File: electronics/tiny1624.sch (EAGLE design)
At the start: 9 parts, among them U1 ATTINY1624

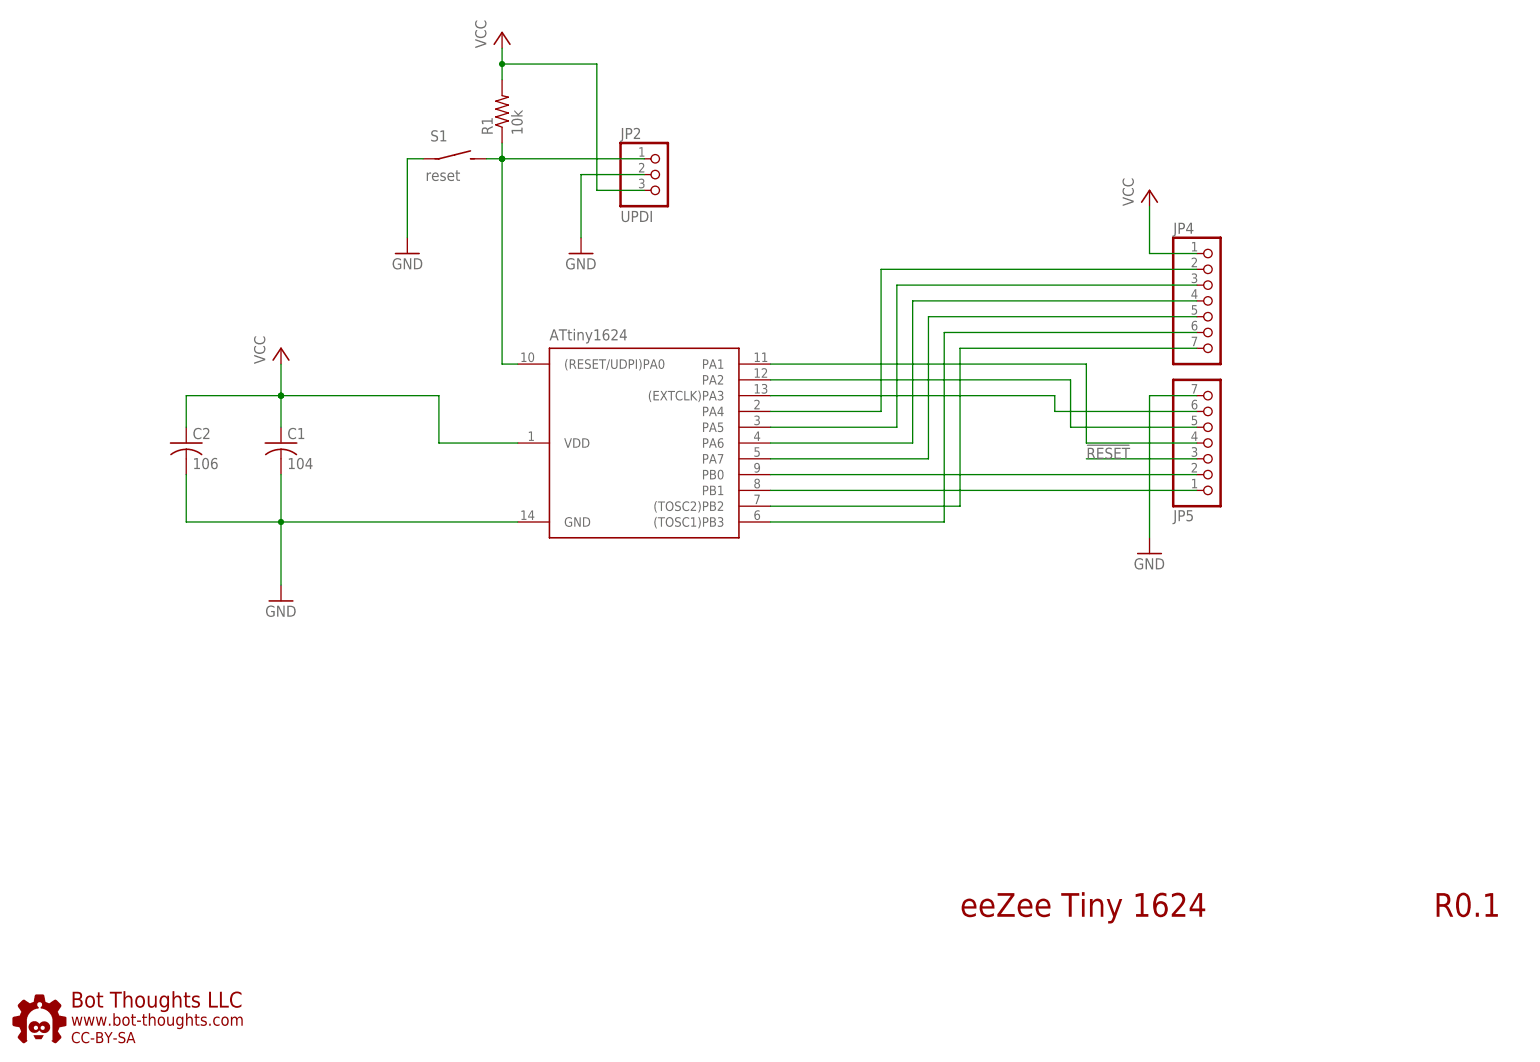
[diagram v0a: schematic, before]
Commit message: Updated reset circuit, added example blink code
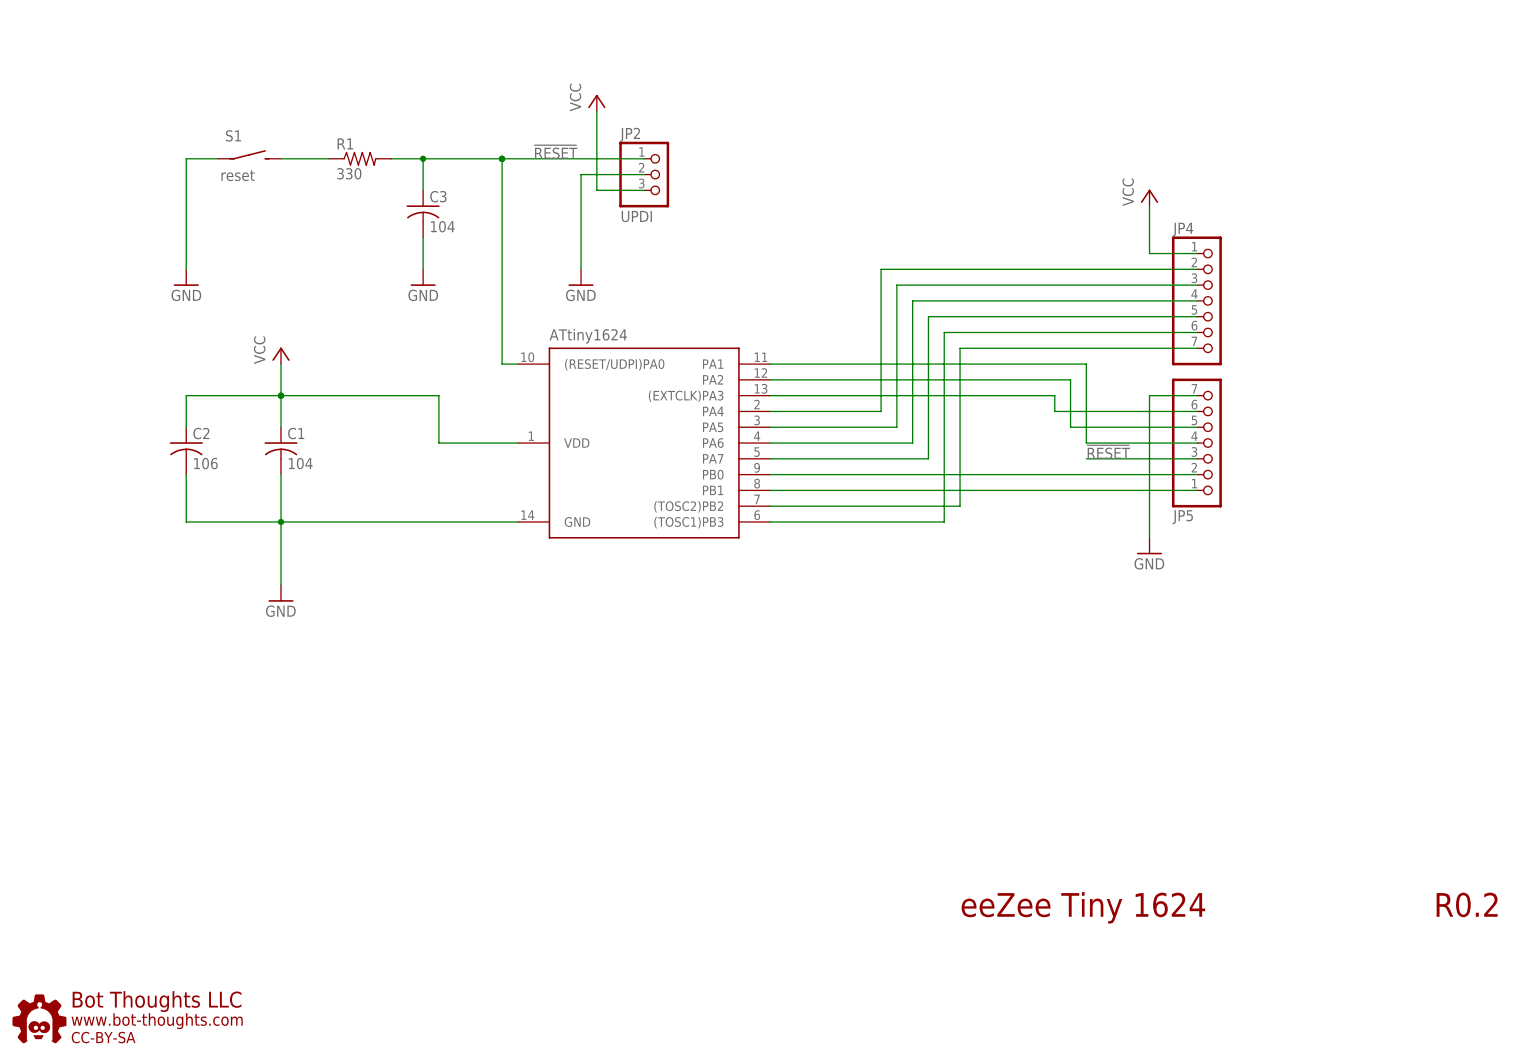
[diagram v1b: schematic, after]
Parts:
- added C3: 104, bt_rcl:C-0603
- R1: value 10k -> 330
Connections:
- new net N$12: R1.1, S1.S
- net !RESET: now also C3.+, R1.2; no longer R1.1, S1.S
- net GND: now also C3.-
- net VCC: no longer R1.2
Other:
- note added: "R0.2"
- note removed: "R0.1"
- moved on the sheet: R1, S1
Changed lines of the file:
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@@
 <part name="GND3" library="supply1" deviceset="GND" device=""/>
 <part name="P+2" library="supply1" deviceset="VCC" device=""/>
-<part name="R1" library="rcl" deviceset="R-US_" device="R0603" value="10k">
+<part name="R1" library="rcl" deviceset="R-US_" device="R0603" value="330">
 <attribute name="PARTNO" value="ERJ-3GEYJ103V"/>
 </part>
@@
 <part name="U1" library="bt_avr" deviceset="ATTINY1624" device="-SSU" value="ATTINY1624"/>
 <part name="JP2" library="pinhead-2" deviceset="PINHD-1X03" device="_2.54-S" value="UPDI"/>
+<part name="C3" library="bt_rcl" deviceset="C" device="-0603" value="104">
+<attribute name="BOM" value="EXCLUDE"/>
+<attribute name="PARTNO" value="0603YC104KAT2A"/>
+</part>
+<part name="GND1" library="supply1" deviceset="GND" device=""/>
 </parts>
 <sheets>
@@
 <plain>
 <text x="154.94" y="22.86" size="3.81" layer="94">eeZee Tiny 1624</text>
-<text x="231.14" y="22.86" size="3.81" layer="94">R0.1</text>
+<text x="231.14" y="22.86" size="3.81" layer="94">R0.2</text>
 </plain>
 <instances>
-<instance part="P+1" gate="VCC" x="81.28" y="165.1"/>
-<instance part="GND2" gate="1" x="93.98" y="129.54"/>
+<instance part="P+1" gate="VCC" x="96.52" y="154.94"/>
+<instance part="GND2" gate="1" x="93.98" y="124.46"/>
 <instance part="C1" gate="G$1" x="45.72" y="99.06">
 <attribute name="PARTNO" value="0603YC104KAT2A" x="45.72" y="99.06" size="1.778" layer="96" display="off"/>
 <attribute name="BOM" value="EXCLUDE" x="45.72" y="99.06" size="1.778" layer="96" display="off"/>
 </instance>
-<instance part="GND3" gate="1" x="66.04" y="129.54" rot="MR0"/>
+<instance part="GND3" gate="1" x="30.48" y="124.46" rot="MR0"/>
 <instance part="P+2" gate="VCC" x="45.72" y="114.3"/>
-<instance part="R1" gate="G$1" x="81.28" y="152.4" rot="R90">
-<attribute name="PARTNO" value="ERJ-3GEYJ103V" x="81.28" y="152.4" size="1.778" layer="96" display="off"/>
+<instance part="R1" gate="G$1" x="58.42" y="144.78">
+<attribute name="PARTNO" value="ERJ-3GEYJ103V" x="58.42" y="144.78" size="1.778" layer="96" rot="R270" display="off"/>
 </instance>
 <instance part="P+4" gate="VCC" x="185.42" y="139.7"/>
@@
 <instance part="JP5" gate="A" x="195.58" y="99.06" rot="MR180"/>
 <instance part="GND4" gate="1" x="185.42" y="81.28"/>
-<instance part="S1" gate="S1" x="73.66" y="144.78"/>
+<instance part="S1" gate="S1" x="40.64" y="144.78"/>
 <instance part="U$1" gate="G$1" x="2.54" y="2.54"/>
 <instance part="U1" gate="G$1" x="104.14" y="99.06"/>
 <instance part="JP2" gate="A" x="106.68" y="142.24"/>
+<instance part="C3" gate="C1" x="68.58" y="137.16">
+<attribute name="PARTNO" value="0603YC104KAT2A" x="68.58" y="137.16" size="1.778" layer="96" display="off"/>
+<attribute name="BOM" value="EXCLUDE" x="68.58" y="137.16" size="1.778" layer="96" display="off"/>
+</instance>
+<instance part="GND1" gate="1" x="68.58" y="124.46" rot="MR0"/>
 </instances>
 <busses>
@@
 <net name="GND" class="0">
 <segment>
-<wire x1="93.98" y1="142.24" x2="93.98" y2="132.08" width="0.1524" layer="91"/>
+<wire x1="93.98" y1="142.24" x2="93.98" y2="127" width="0.1524" layer="91"/>
 <pinref part="GND2" gate="1" pin="GND"/>
 <pinref part="JP2" gate="A" pin="2"/>
@@
 <segment>
 <pinref part="GND3" gate="1" pin="GND"/>
-<wire x1="68.58" y1="144.78" x2="66.04" y2="144.78" width="0.1524" layer="91"/>
-<wire x1="66.04" y1="144.78" x2="66.04" y2="132.08" width="0.1524" layer="91"/>
+<wire x1="35.56" y1="144.78" x2="30.48" y2="144.78" width="0.1524" layer="91"/>
+<wire x1="30.48" y1="144.78" x2="30.48" y2="127" width="0.1524" layer="91"/>
 <pinref part="S1" gate="S1" pin="P"/>
 </segment>
@@
 <wire x1="185.42" y1="106.68" x2="185.42" y2="83.82" width="0.1524" layer="91"/>
 <pinref part="GND4" gate="1" pin="GND"/>
+</segment>
+<segment>
+<pinref part="C3" gate="C1" pin="-"/>
+<pinref part="GND1" gate="1" pin="GND"/>
+<wire x1="68.58" y1="127" x2="68.58" y2="132.08" width="0.1524" layer="91"/>
 </segment>
 </net>
@@
 </segment>
 <segment>
-<wire x1="81.28" y1="157.48" x2="81.28" y2="160.02" width="0.1524" layer="91"/>
 <pinref part="P+1" gate="VCC" pin="VCC"/>
-<pinref part="R1" gate="G$1" pin="2"/>
 <pinref part="JP2" gate="A" pin="3"/>
-<wire x1="81.28" y1="160.02" x2="81.28" y2="162.56" width="0.1524" layer="91"/>
 <wire x1="104.14" y1="139.7" x2="96.52" y2="139.7" width="0.1524" layer="91"/>
-<wire x1="96.52" y1="139.7" x2="96.52" y2="160.02" width="0.1524" layer="91"/>
-<wire x1="81.28" y1="160.02" x2="96.52" y2="160.02" width="0.1524" layer="91"/>
-<junction x="81.28" y="160.02"/>
+<wire x1="96.52" y1="139.7" x2="96.52" y2="152.4" width="0.1524" layer="91"/>
 </segment>
 <segment>
@@
 <net name="!RESET" class="0">
 <segment>
-<wire x1="81.28" y1="144.78" x2="81.28" y2="147.32" width="0.1524" layer="91"/>
 <junction x="81.28" y="144.78"/>
-<pinref part="R1" gate="G$1" pin="1"/>
 <wire x1="104.14" y1="144.78" x2="81.28" y2="144.78" width="0.1524" layer="91"/>
-<wire x1="78.74" y1="144.78" x2="81.28" y2="144.78" width="0.1524" layer="91"/>
 <junction x="81.28" y="144.78"/>
-<pinref part="S1" gate="S1" pin="S"/>
 <pinref part="U1" gate="G$1" pin="(RESET/UDPI)PA0"/>
+<wire x1="63.5" y1="144.78" x2="68.58" y2="144.78" width="0.1524" layer="91"/>
+<wire x1="68.58" y1="144.78" x2="81.28" y2="144.78" width="0.1524" layer="91"/>
 <wire x1="83.82" y1="111.76" x2="81.28" y2="111.76" width="0.1524" layer="91"/>
 <wire x1="81.28" y1="111.76" x2="81.28" y2="144.78" width="0.1524" layer="91"/>
 <pinref part="JP2" gate="A" pin="1"/>
+<pinref part="R1" gate="G$1" pin="2"/>
+<pinref part="C3" gate="C1" pin="+"/>
+<wire x1="68.58" y1="139.7" x2="68.58" y2="144.78" width="0.1524" layer="91"/>
+<junction x="68.58" y="144.78"/>
+<label x="86.36" y="144.78" size="1.778" layer="95"/>
 </segment>
 <segment>
@@
 </segment>
 </net>
+<net name="N$12" class="0">
+<segment>
+<pinref part="R1" gate="G$1" pin="1"/>
+<wire x1="45.72" y1="144.78" x2="53.34" y2="144.78" width="0.1524" layer="91"/>
+<pinref part="S1" gate="S1" pin="S"/>
+</segment>
+</net>

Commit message: Removed reset circuit, shrunk board, cleaned up schematic
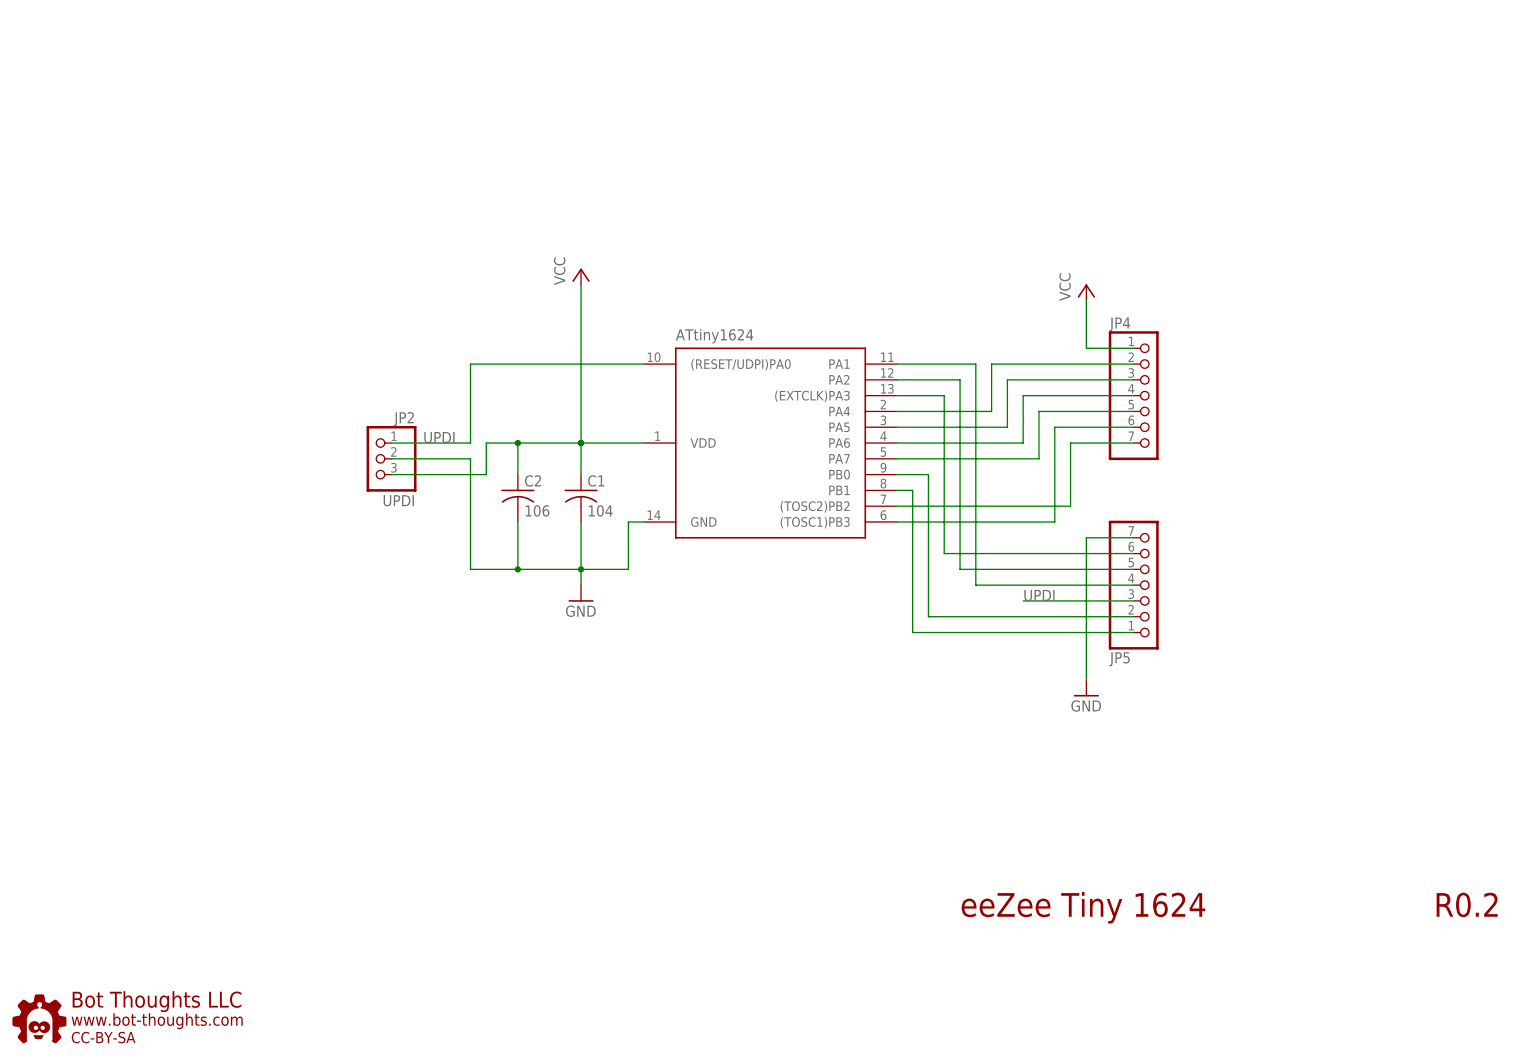
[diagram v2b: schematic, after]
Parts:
- removed C3: 104, bt_rcl:C-0603
- removed R1: 330, rcl:R-US_R0603
- removed S1: reset, bt_electromech:SPST_3X4X2
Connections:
- removed net !RESET: C3.+, JP2.1, JP5.3, R1.2, U1.(RESET/UDPI)PA0
- removed net N$12: R1.1, S1.S
- new net UPDI: JP2.1, JP5.3, U1.(RESET/UDPI)PA0
- net GND: no longer C3.-, S1.P
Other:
- moved on the sheet: C1, C2, JP2, JP4, JP5
